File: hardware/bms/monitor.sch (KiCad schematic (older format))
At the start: 71 parts

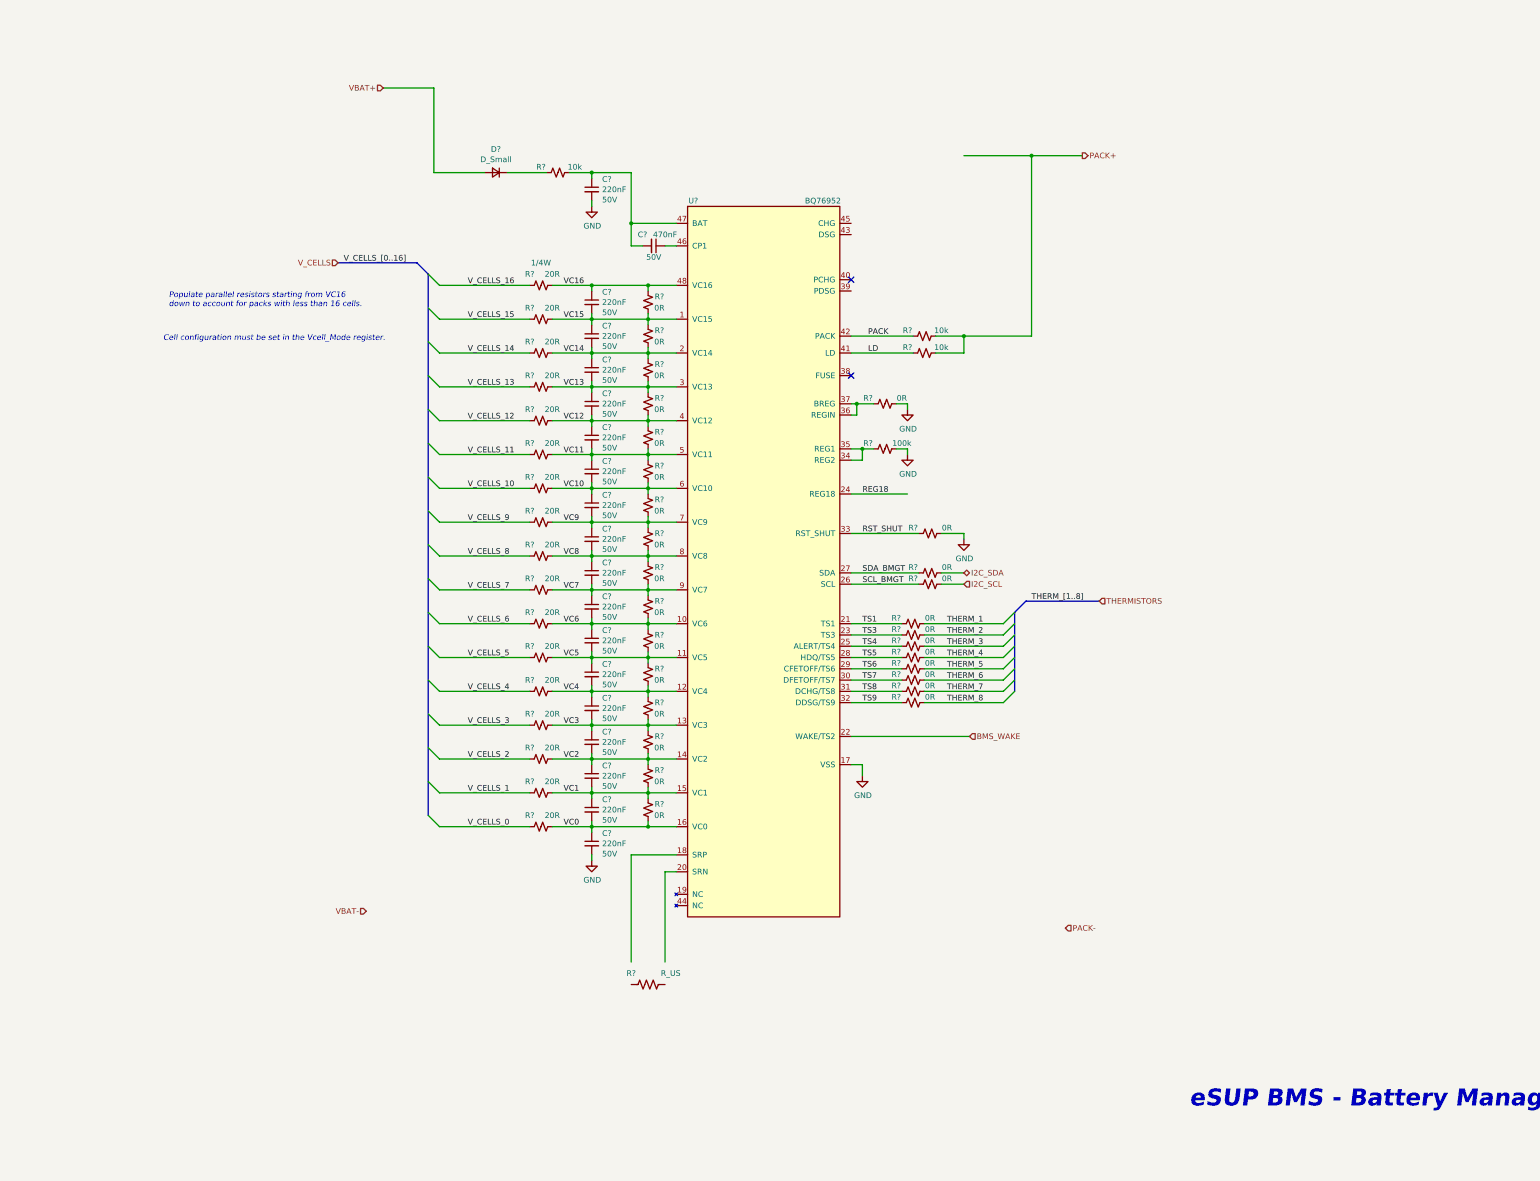
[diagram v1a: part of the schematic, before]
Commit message: Battery monitor / balancer schematic complete. Charger is next. Thinking of adding MCU directly to this board if layout space allows, probably doesn't deserve its own board (or just deserves a dev board)
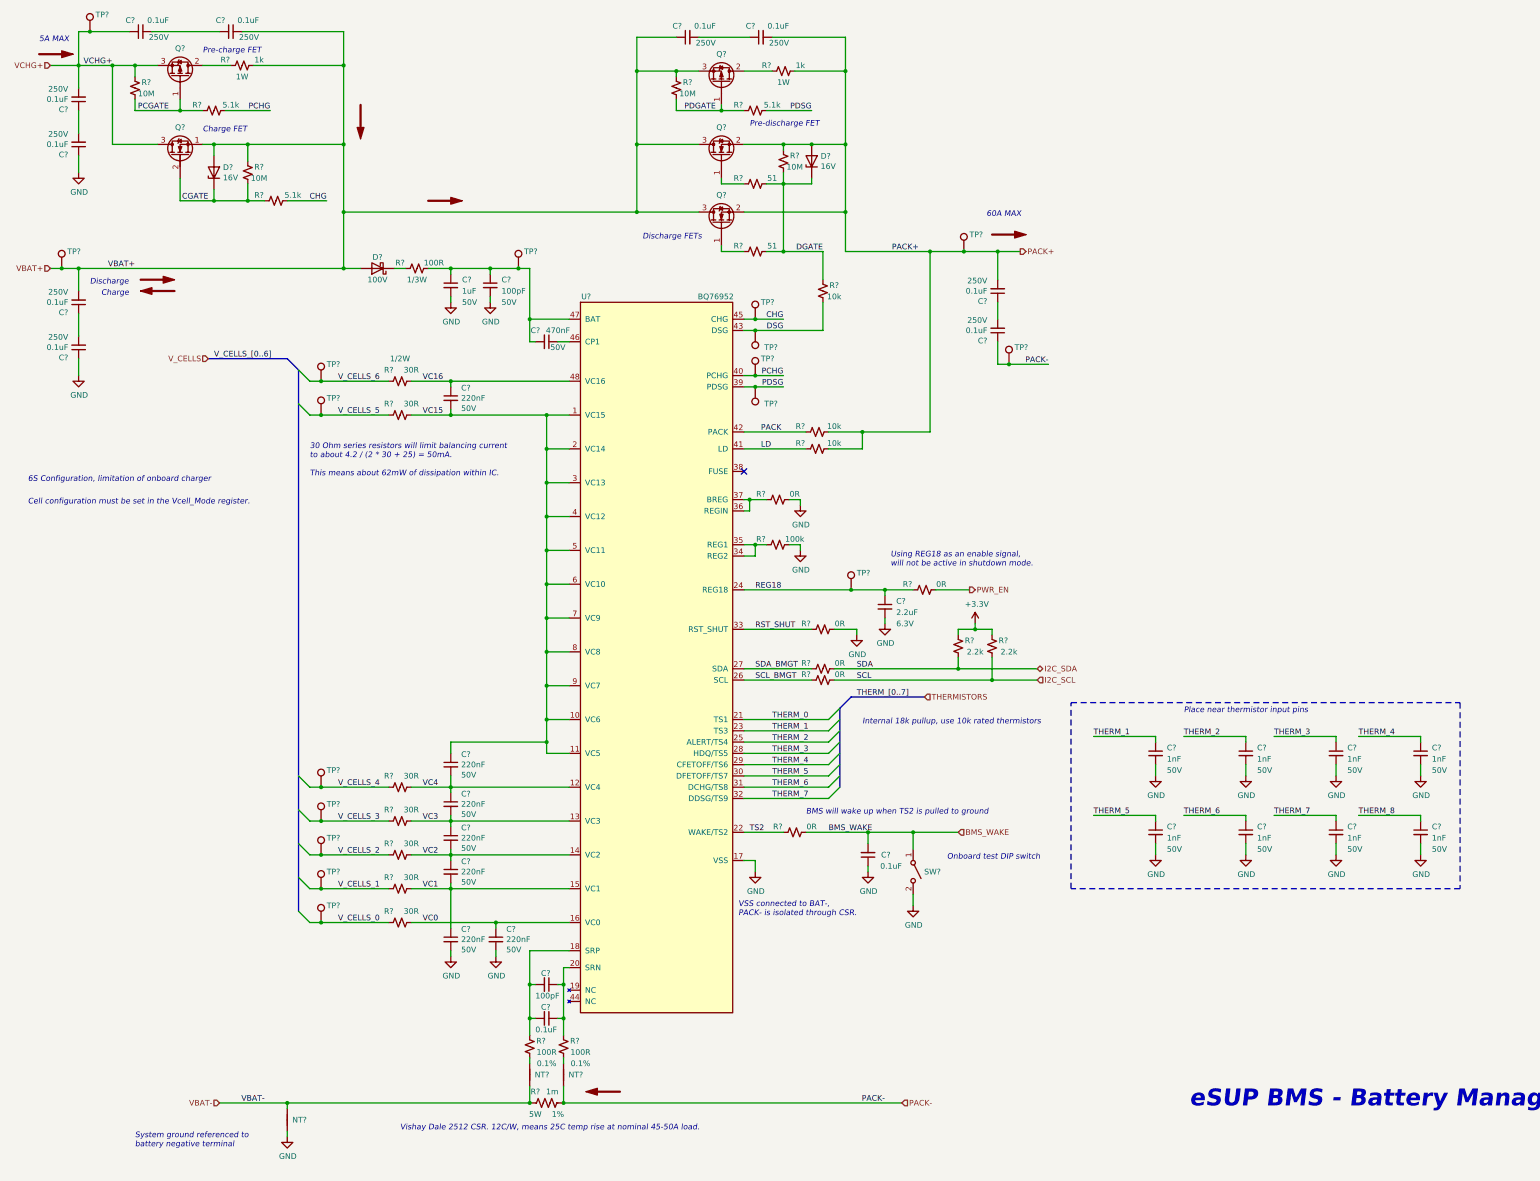
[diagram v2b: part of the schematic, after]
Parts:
- removed C? (x10): 220nF, symbol Device:C_Small
- removed D?: D_Small, symbol Device:D_Small
- removed R? (x24): 0R, symbol Device:R_Small_US
- removed R? (x16): 20R, symbol Device:R_Small_US
- added C? (x10): 0.1uF, Capacitor_SMD:C_0805_2012Metric, symbol Device:C_Small
- added C? (x2): 100pF, Capacitor_SMD:C_0603_1608Metric, symbol Device:C_Small
- added C?: 2.2uF, Capacitor_SMD:C_0603_1608Metric, symbol Device:C_Small
- added C? (x8): 1nF, Capacitor_SMD:C_0603_1608Metric, symbol Device:C_Small
- added C? (x2): 0.1uF, Capacitor_SMD:C_0603_1608Metric, symbol Device:C_Small
- added D?: D_Schottky, Diode_SMD:D_SOD-123, symbol Device:D_Schottky
- added D? (x2): D_Zener, Diode_SMD:D_SOD-123, symbol Device:D_Zener
- added NT? (x2): Net-Tie, NetTie:NetTie-2_SMD_Pad0.5mm, symbol Device:Net-Tie_2
- added NT?: Net-Tie, NetTie:NetTie-2_SMD_Pad2.0mm, symbol Device:Net-Tie_2
- added Q? (x2): Q_PMOS_GDS, Package_TO_SOT_SMD:SOT-223-3_TabPin2, symbol Device:Q_PMOS_GDS
- added Q? (x2): Q_NMOS_GSD, Package_TO_SOT_SMD:Infineon_PG-HSOF-8-1, symbol Device:Q_NMOS_GSD
- added Q?: Q_NMOS_SGD, bms:PG-TDSON-8, symbol Device:Q_NMOS_SGD
- added R? (x3): 5.1k, Resistor_SMD:R_0603_1608Metric, symbol Device:R_Small_US
- added R? (x2): 51, Resistor_SMD:R_0603_1608Metric, symbol Device:R_Small_US
- added R?: 10k, Resistor_SMD:R_0603_1608Metric, symbol Device:R_Small_US
- added R? (x2): 0R, Resistor_SMD:R_0603_1608Metric, symbol Device:R_Small_US
- added R? (x4): 10M, Resistor_SMD:R_0603_1608Metric, symbol Device:R_Small_US
- added R? (x2): 1k, Resistor_SMD:R_2512_6332Metric, symbol Device:R_Small_US
- added R? (x6): 30R, Resistor_SMD:R_1210_3225Metric, symbol Device:R_Small_US
- added R? (x2): 2.2k, Resistor_SMD:R_0603_1608Metric, symbol Device:R_Small_US
- added R? (x2): 100R, Resistor_SMD:R_0603_1608Metric, symbol Device:R_Small_US
- added SW?: SW_SPST, bms:SW_DS04-254-2-01BK-SMT-TR, symbol Switch:SW_SPST
- added TP? (x17): TestPoint, TestPoint:TestPoint_Pad_D1.0mm, symbol Connector:TestPoint
- C?: footprint (none) -> Capacitor_SMD:C_0603_1608Metric
- C?: value 220nF -> 1uF; footprint (none) -> Capacitor_SMD:C_0805_2012Metric; MFG PN GCJ188R71H224KA01D -> GCM21BR71H105KA03K
- R?: value 20R -> 30R; footprint (none) -> Resistor_SMD:R_1210_3225Metric; MFG PN ERJ-UP3F20R0V -> ERJ-P14J300U; Power 1/4W -> 1/2W
- R?: value R_US -> 1m; footprint (none) -> Resistor_SMD:R_2512_6332Metric; MFG (none) -> Vishay Dale; MFG PN (none) -> WSLF25121L000FEB; Power (none) -> 5W; Tolerance (none) -> 1%
- R? (x7): footprint (none) -> Resistor_SMD:R_0603_1608Metric
- R?: value 10k -> 100R; footprint (none) -> Resistor_SMD:R_0603_1608Metric; MFG PN ERJ-3GEYJ103V -> ERJ-PA3J101V; Power (none) -> 1/3W
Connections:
- net TS3 is gone; now on net THERM_1: U?.23 (TS3)
- net TS4 is gone; now on net THERM_2: U?.25 (ALERT/TS4)
- net TS5 is gone; now on net THERM_3: U?.28 (HDQ/TS5)
- net TS6 is gone; now on net THERM_4: U?.29 (CFETOFF/TS6)
- net TS7 is gone; now on net THERM_5: U?.30 (DFETOFF/TS7)
- net TS8 is gone; now on net THERM_6: U?.31 (DCHG/TS8)
- net TS9 is gone; now on net THERM_7: U?.32 (DDSG/TS9)
- net VC10 is gone; now on net VC15: U?.6 (VC10)
- net VC11 is gone; now on net VC15: U?.5 (VC11)
- net VC12 is gone; now on net VC15: U?.4 (VC12)
- net VC13 is gone; now on net VC15: U?.3 (VC13)
- net VC14 is gone; now on net VC15: U?.2 (VC14)
- net VC5 is gone; now on net VC15: C?.1, U?.11 (VC5)
- net VC6 is gone; now on net VC15: U?.10 (VC6)
- net VC7 is gone; now on net VC15: U?.9 (VC7)
- net VC8 is gone; now on net VC15: U?.8 (VC8)
- net VC9 is gone; now on net VC15: U?.7 (VC9)
- net V_CELLS_16 is gone; now on net V_CELLS_6: R?.2
- net BMS_WAKE: now also C?.2, R?.2, SW?.1 (A); no longer U?.22 (WAKE/TS2)
- net GND: now also C?.2, C?.1, C?.1, C?.1, C?.2, C?.2, C?.2, C?.2, C?.2, C?.2, C?.2, C?.2, C?.2, C?.2, NT?.2, SW?.2 (B)
- net I2C_SCL: now also R?.2
- net I2C_SDA: now also R?.2
- net PACK+: now also C?.2, C?.2, D?.2 (A), Q?.2 (S), Q?.2 (S), R?.1, R?.2, TP?.1
- net PACK-: now also R?.1, C?.1, NT?.2, TP?.1
- net REG18: now also C?.1, R?.1, TP?.1
- net THERM_1: now also C?.1
- net THERM_2: now also C?.1
- net THERM_3: now also C?.1
- net THERM_4: now also C?.1
- net THERM_5: now also C?.1
- net THERM_6: now also C?.1
- net THERM_7: now also C?.1
- net THERM_8: now also C?.1
- net VBAT+: now also C?.1, C?.2, C?.2, D?.2 (A), D?.2 (A), Q?.1 (S), Q?.3 (D), Q?.3 (D), Q?.3 (S), R?.1, R?.1, R?.2, TP?.1
- net VBAT-: now also R?.2, NT?.1, NT?.2
- net VC0: now also R?.1; no longer C?.2
- net VC1: now also R?.1
- net VC15: now also R?.1
- net VC2: now also R?.1
- net VC3: now also R?.1
- net VC4: now also R?.1
- net V_CELLS_0: now also R?.2, TP?.1
- net V_CELLS_1: now also R?.2, TP?.1
- net V_CELLS_2: now also R?.2, TP?.1
- net V_CELLS_3: now also R?.2, TP?.1
- net V_CELLS_4: now also R?.2, TP?.1
- net V_CELLS_5: now also R?.2, TP?.1
- net V_CELLS_6: now also TP?.1
- net at U?.18 (SRP): now also C?.2, C?.2, R?.1
- net at U?.20 (SRN): now also C?.1, C?.1, R?.1
- net PDSG: now reaches U?.39 (PDSG)
- net PDSG: now also R?.2, TP?.1
- net PCHG: now reaches U?.40 (PCHG)
- net PCHG: now also R?.2, TP?.1
- net DSG: now reaches U?.43 (DSG)
- net DSG: now also R?.2, TP?.1
- net CHG: now reaches U?.45 (CHG)
- net CHG: now also R?.2, TP?.1
- net at C?.1, C?.2, R?.2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: now also C?.1, TP?.1
- net at R?.1: now also D?.1 (K)
- net TS1 renamed THERM_0
- new net: C?.1, C?.2 (x5)
- new net: Q?.1 (G), R?.1 (x2)
- new net: Q?.2 (D), R?.1 (x2)
- new net: NT?.1, R?.2 (x2)
- new net +3V3: R?.1, R?.1
- new net CGATE: D?.1 (K), Q?.2 (G), R?.1, R?.2
- new net DGATE: D?.1 (K), R?.1, R?.2, R?.2, R?.2
- new net PCGATE: Q?.1 (G), R?.1, R?.2
- new net PDGATE: Q?.1 (G), R?.1, R?.2
- new net PWR_EN: R?.2
- new net TS2: R?.1, U?.22 (WAKE/TS2)
- new net VCHG+: C?.1, C?.2, Q?.3 (D), Q?.3 (S), R?.1, TP?.1
- no-connect marks 2 -> 1
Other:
- note added: "30 Ohm series resistors will limit balancing current \nto about 4.2 / (2 * 30 + 25) = 50mA.\n\nThis means about 62mW of dissipation within IC.\n"
- note added: "5A MAX"
- note added: "60A MAX"
- note added: "6S Configuration, limitation of onboard charger"
- note added: "BMS will wake up when TS2 is pulled to ground"
- note added: "Charge"
- note added: "Charge FET"
- note added: "Discharge"
- note added: "Discharge FETs"
- note added: "Internal 18k pullup, use 10k rated thermistors"
- note added: "Onboard test DIP switch"
- note added: "Place near thermistor input pins"
- note added: "Pre-charge FET"
- note added: "Pre-discharge FET"
- note added: "System ground referenced to \nbattery negative terminal"
- note added: "Using REG18 as an enable signal, \nwill not be active in shutdown mode."
- note added: "VSS connected to BAT-, \nPACK- is isolated through CSR."
- note added: "Vishay Dale 2512 CSR. 12C/W, means 25C temp rise at nominal 45-50A load."
- note removed: "Populate parallel resistors starting from VC16 \ndown to account for packs with less than 16 cells."
- moved on the sheet: C?, R?, U?

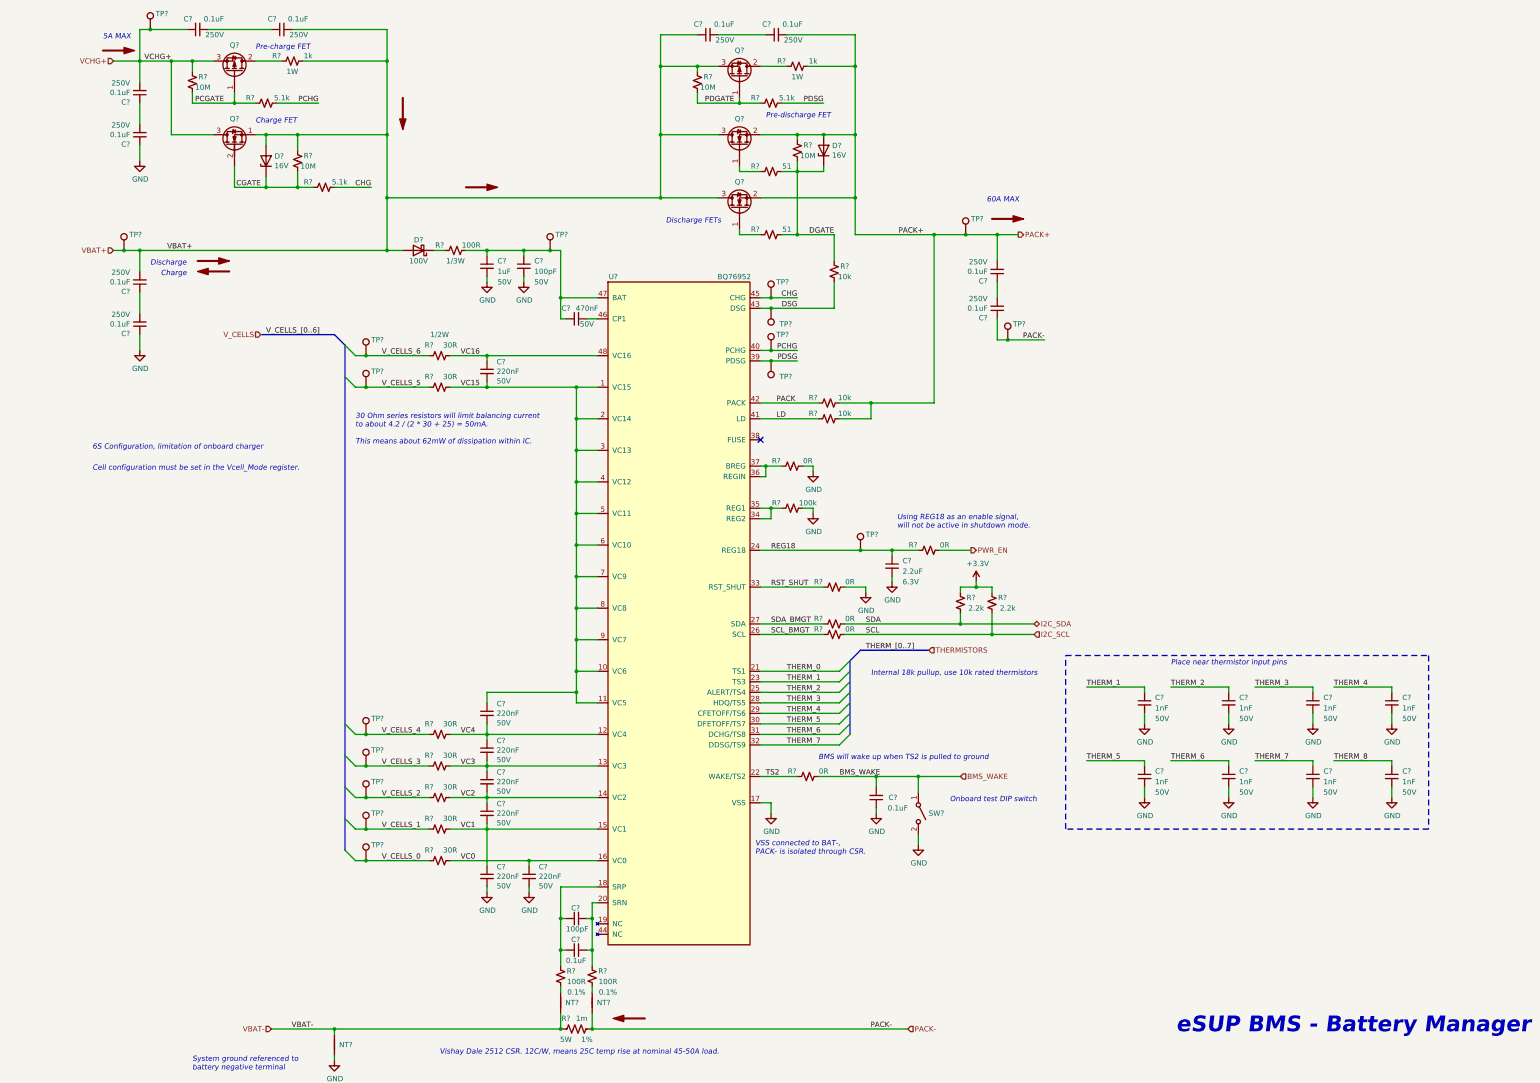
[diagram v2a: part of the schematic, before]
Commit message: Created footprints for microfit and wurth screw terminals
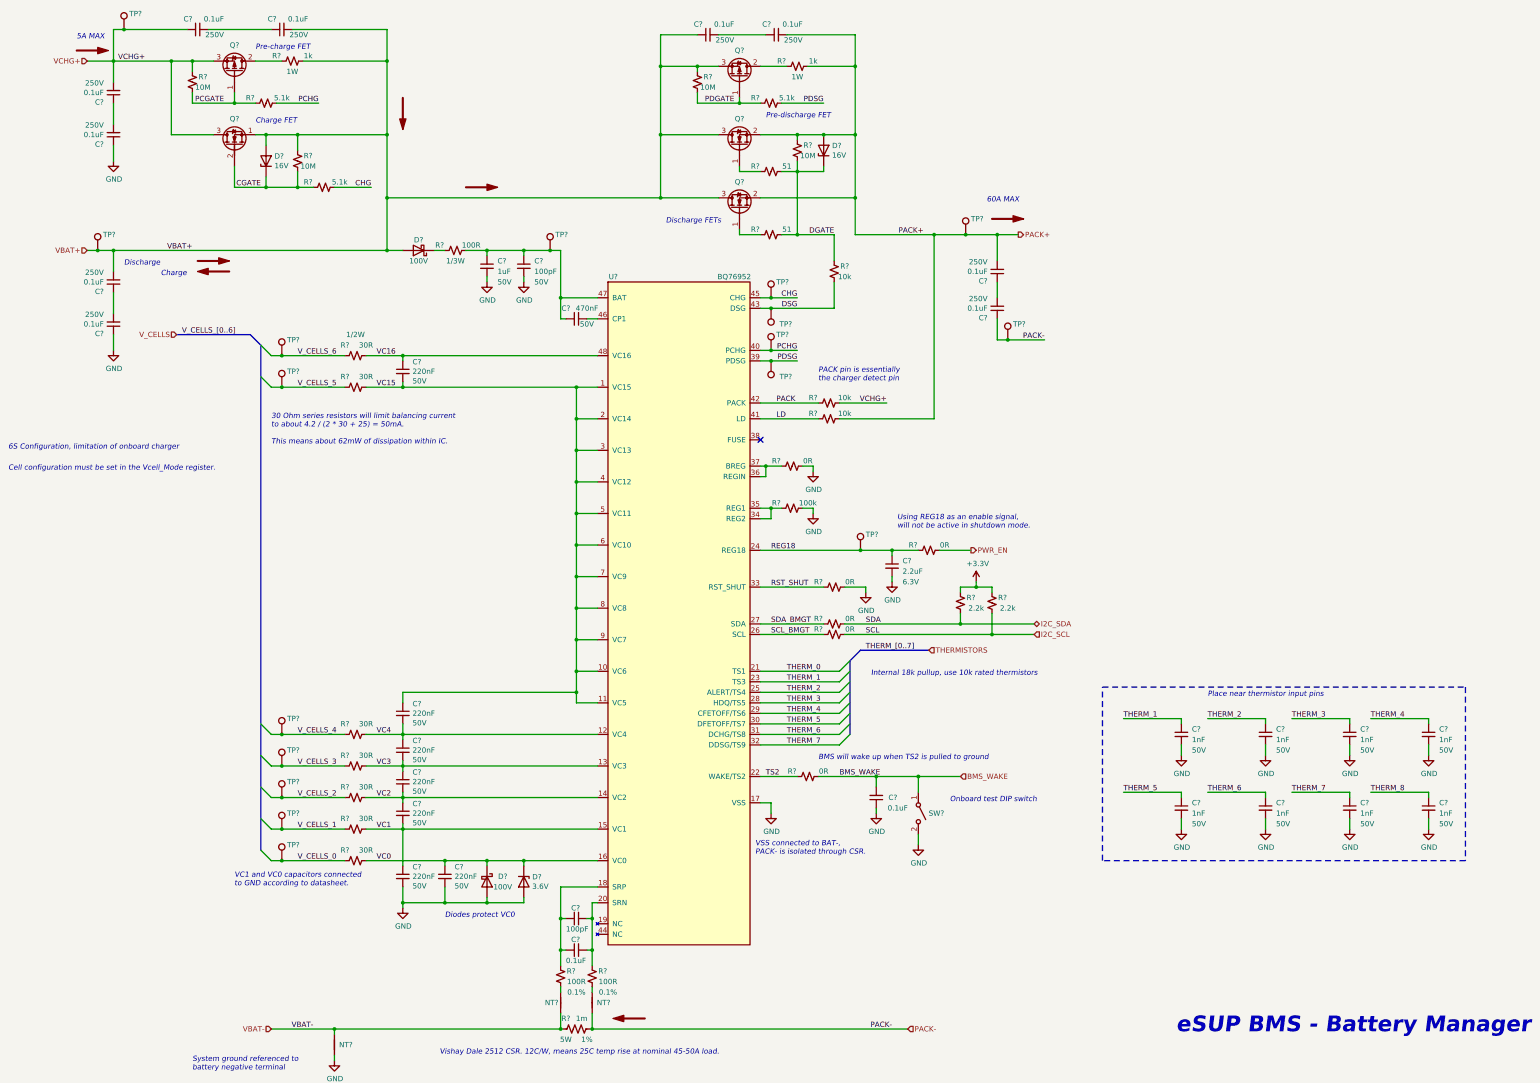
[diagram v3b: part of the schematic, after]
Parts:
- added D?: D_Schottky, Diode_SMD:D_SOD-123, symbol Device:D_Schottky
- added D?: D_Zener, Diode_SMD:D_SOD-123, symbol Device:D_Zener
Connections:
- net GND: now also D?.2 (A), D?.2 (A)
- net PACK+: no longer R?.2
- net VC0: now also D?.1 (K), D?.1 (K)
- net VCHG+: now also R?.2
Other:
- note added: "Diodes protect VC0"
- note added: "PACK pin is essentially\nthe charger detect pin"
- note added: "VC1 and VC0 capacitors connected \nto GND according to datasheet."
- moved on the sheet: C?, R?, TP?
